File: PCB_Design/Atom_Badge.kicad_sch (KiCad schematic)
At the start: 4 parts

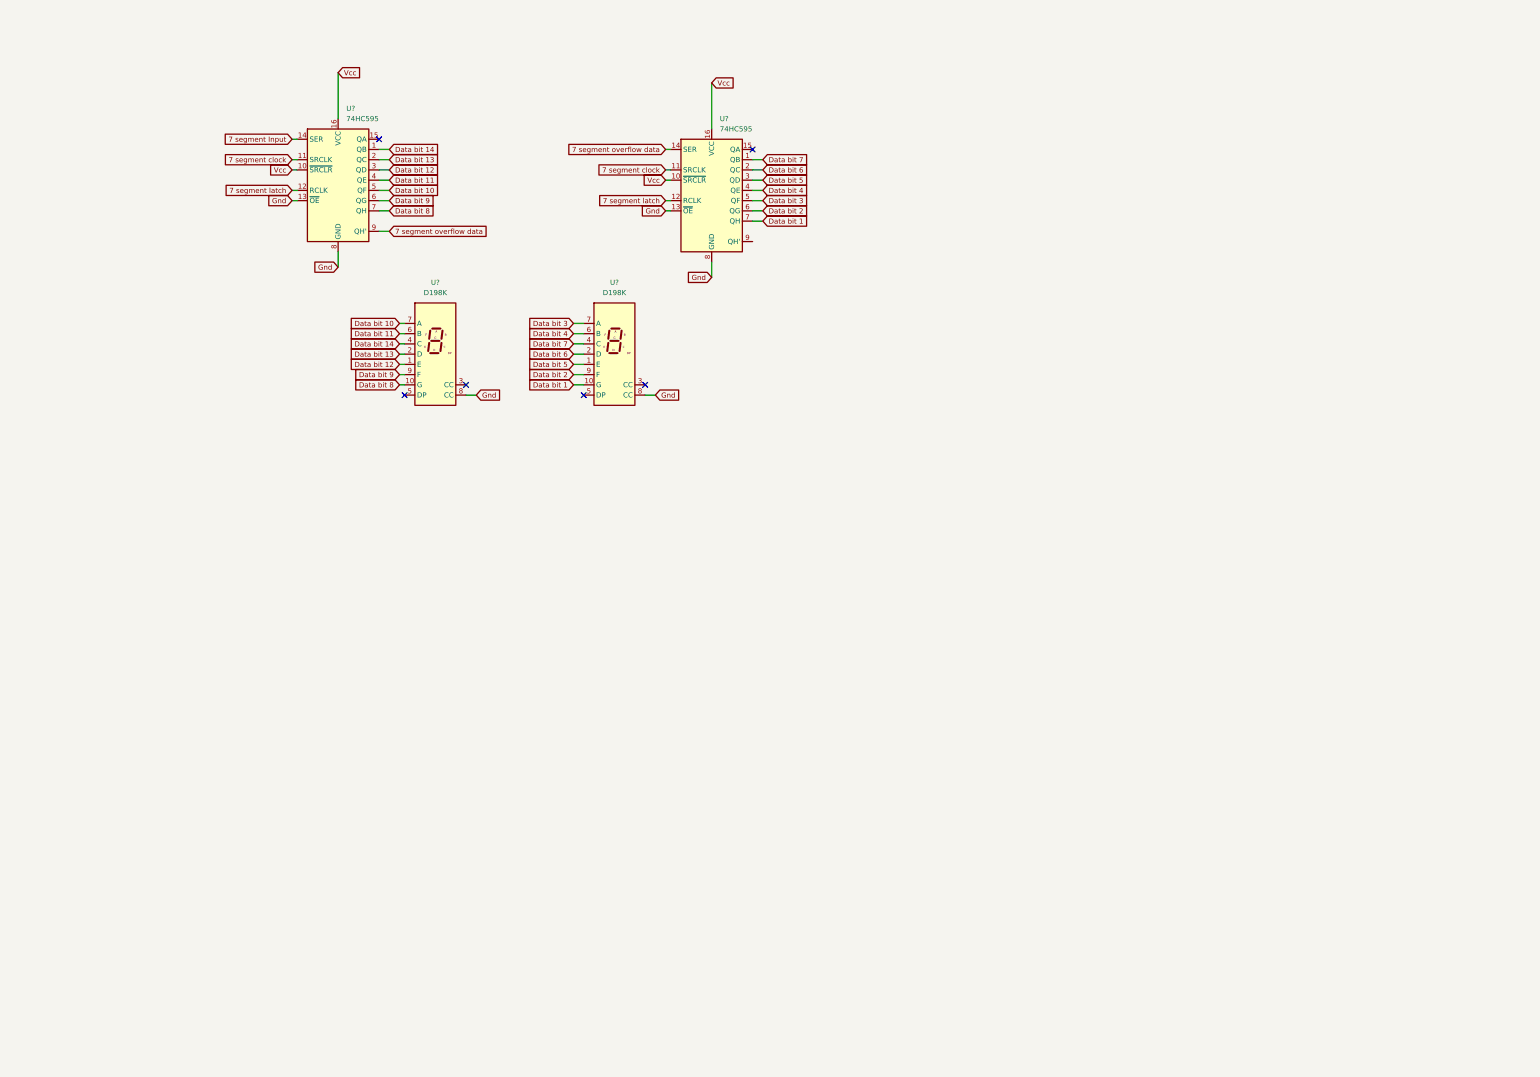
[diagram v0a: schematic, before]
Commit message: Added ESP12E to schematic
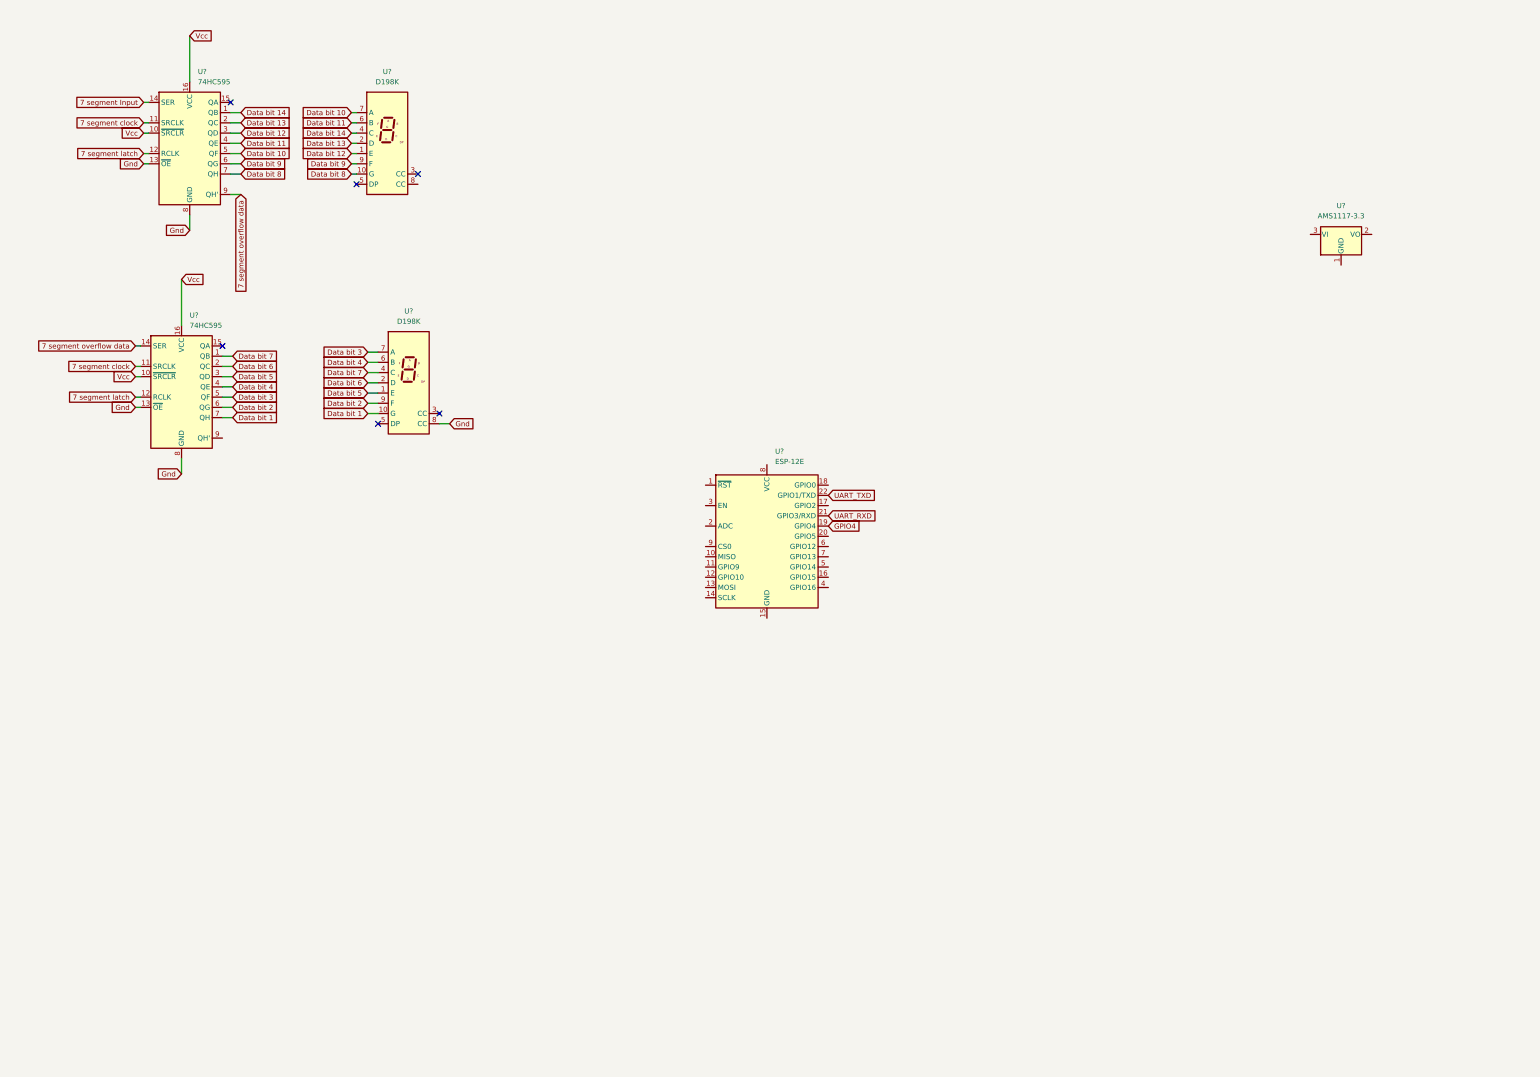
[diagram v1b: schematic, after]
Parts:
- added U?: AMS1117-3.3, Package_TO_SOT_SMD:SOT-223-3_TabPin2, symbol Regulator_Linear:AMS1117-3.3
- added U?: ESP-12E, RF_Module:ESP-12E, symbol RF_Module:ESP-12E
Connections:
- net Gnd: no longer U?.8 (CC)
- new net GPIO4: U?.19 (GPIO4)
- new net UART_RXD: U?.21 (GPIO3/RXD)
- new net UART_TXD: U?.22 (GPIO1/TXD)
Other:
- company: (none) -> A.T.O.M Robotics Lab
- title: (none) -> A.T.O.M PCB Badge
- moved on the sheet: U?

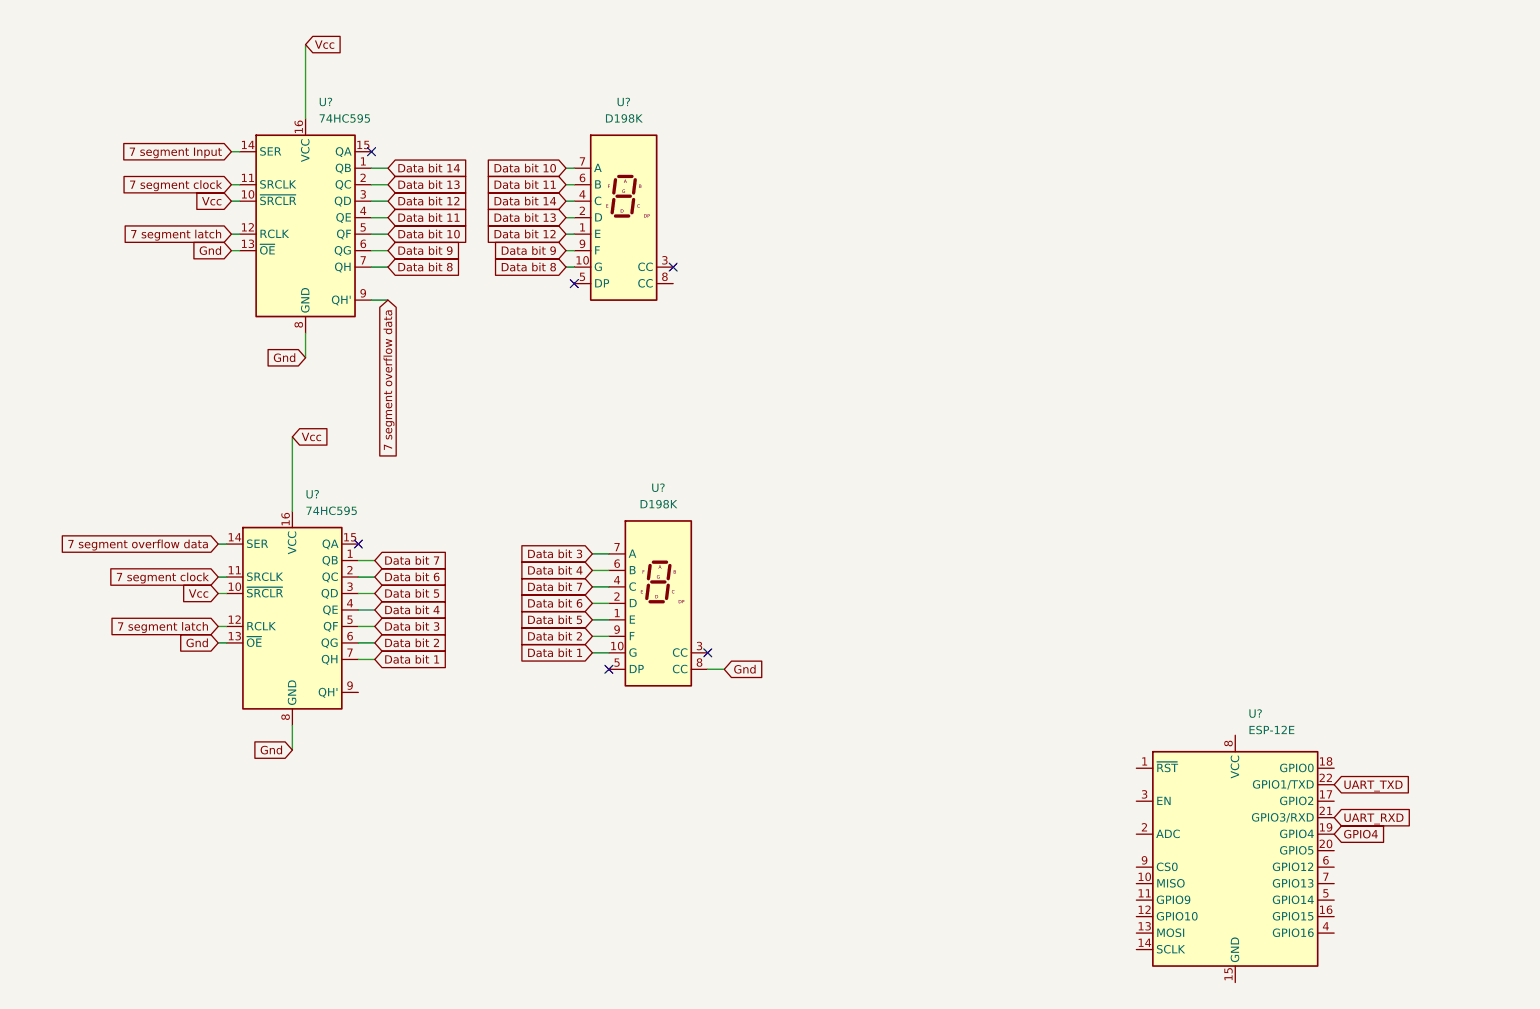
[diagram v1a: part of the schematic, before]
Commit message: changes in 7 segment schematics
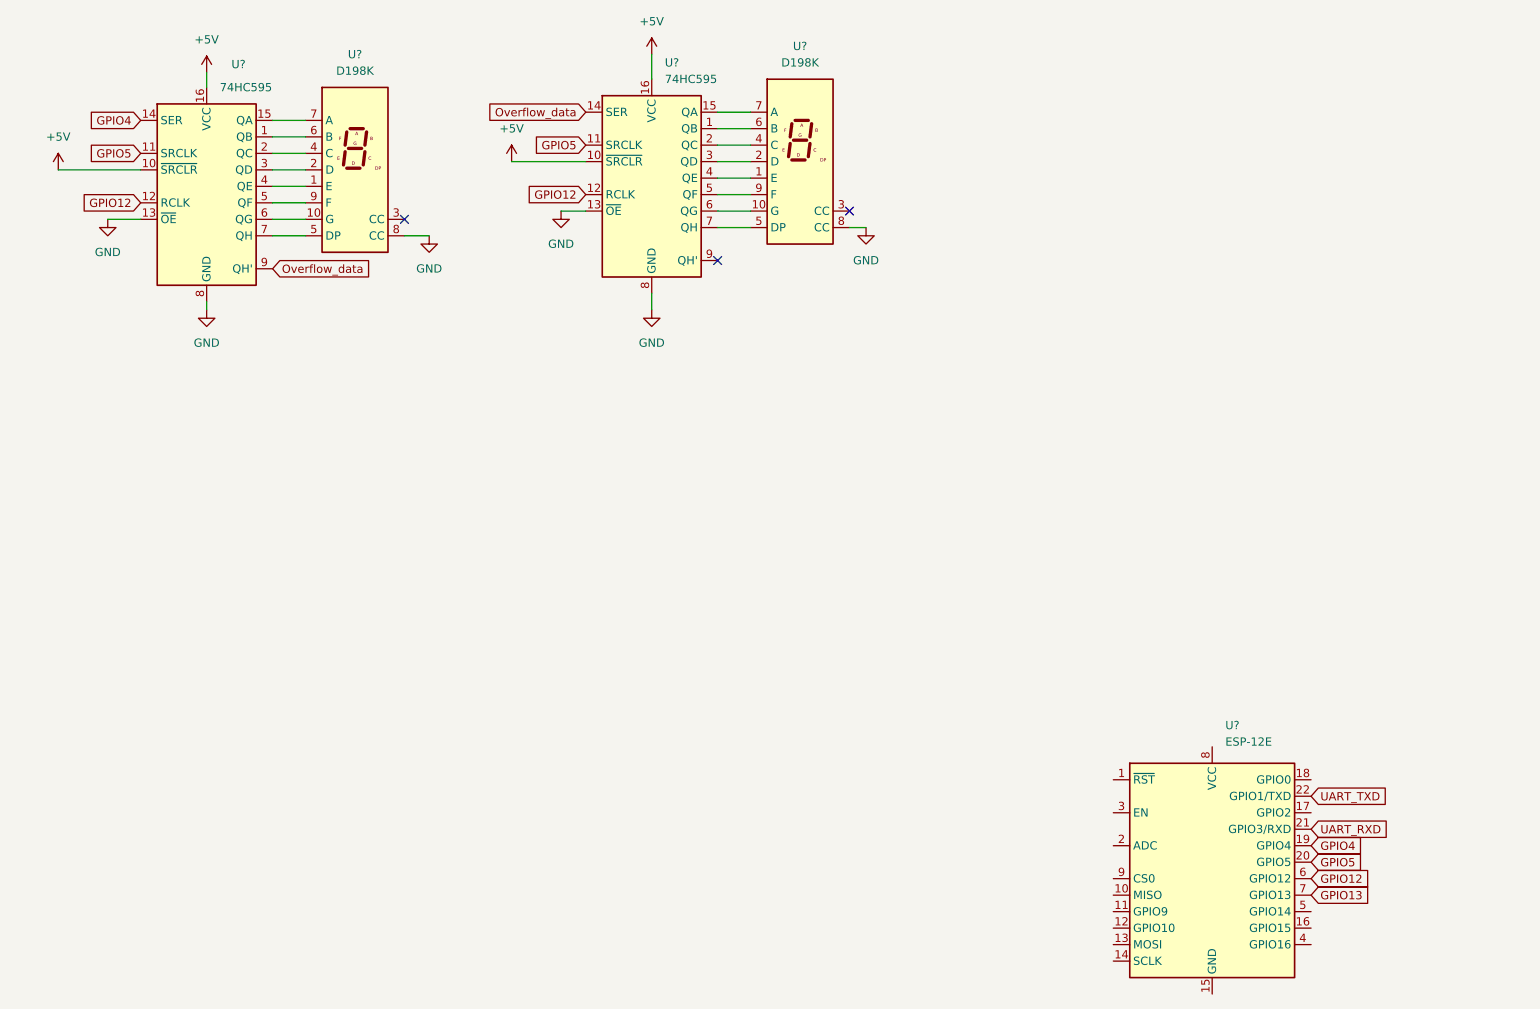
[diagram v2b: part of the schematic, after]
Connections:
- net 7 segment Input  is gone; now on net GPIO4: U?.14 (SER)
- net 7 segment clock is gone; now on net GPIO5: U?.11 (SRCLK), U?.11 (SRCLK)
- net 7 segment latch is gone; now on net GPIO12: U?.12 (RCLK), U?.12 (RCLK)
- net Gnd is gone; now on net GND: U?.13 (~{OE}), U?.13 (~{OE}), U?.8 (CC), U?.8 (GND), U?.8 (GND)
- net at U?.15 (QA): now also U?.7 (A) (x2)
- net at U?.5 (DP): now also U?.7 (QH) (x2)
- net GND: now reaches U?.8 (CC)
- net GPIO5: now reaches U?.20 (GPIO5)
- net GPIO12: now reaches U?.6 (GPIO12)
- net GPIO13: now reaches U?.7 (GPIO13)
- net 7 segment overflow data renamed Overflow_data
- net Data bit 1: no longer names the net of U?.10 (G)
- net Data bit 1: now also U?.6 (QG); no longer U?.7 (QH)
- net Data bit 10: no longer names the net of U?.5 (QF)
- net Data bit 10: now also U?.9 (F); no longer U?.7 (A)
- net Data bit 11: no longer names the net of U?.6 (B)
- net Data bit 11: now also U?.1 (QB); no longer U?.4 (QE)
- net Data bit 12: no longer names the net of U?.3 (QD)
- net Data bit 12: now also U?.2 (D); no longer U?.1 (E)
- net Data bit 13: no longer names the net of U?.2 (QC)
- net Data bit 13: now also U?.4 (C); no longer U?.2 (D)
- removed net Data bit 14: U?.1 (QB), U?.4 (C)
- net Data bit 2: no longer names the net of U?.9 (F)
- net Data bit 2: now also U?.5 (QF); no longer U?.6 (QG)
- removed net Data bit 3: U?.5 (QF), U?.7 (A)
- net Data bit 4: no longer names the net of U?.6 (B)
- net Data bit 4: now also U?.1 (QB); no longer U?.4 (QE)
- net Data bit 5: no longer names the net of U?.3 (QD)
- net Data bit 5: now also U?.2 (D); no longer U?.1 (E)
- net Data bit 6: no longer names the net of U?.2 (QC)
- net Data bit 6: now also U?.4 (C); no longer U?.2 (D)
- removed net Data bit 7: U?.1 (QB), U?.4 (C)
- net Data bit 8: no longer names the net of U?.10 (G)
- net Data bit 8: now also U?.6 (QG); no longer U?.7 (QH)
- removed net Data bit 9: U?.6 (QG), U?.9 (F)
- net Vcc renamed +5V
- new net: U?.1 (E), U?.4 (QE) (x2)
- no-connect marks 6 -> 3
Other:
- moved on the sheet: U?
